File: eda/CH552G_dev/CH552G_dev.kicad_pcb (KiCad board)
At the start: 2 copper layers, 34 x 44 mm, 27 parts, among them IC1 CH552G, J1 USB_B_Micro, J2 Test 1-8, J3 Test 9-16, J4 Battery, SW1 TS2306A, SW11 TS2306A, SW34 TS2306A

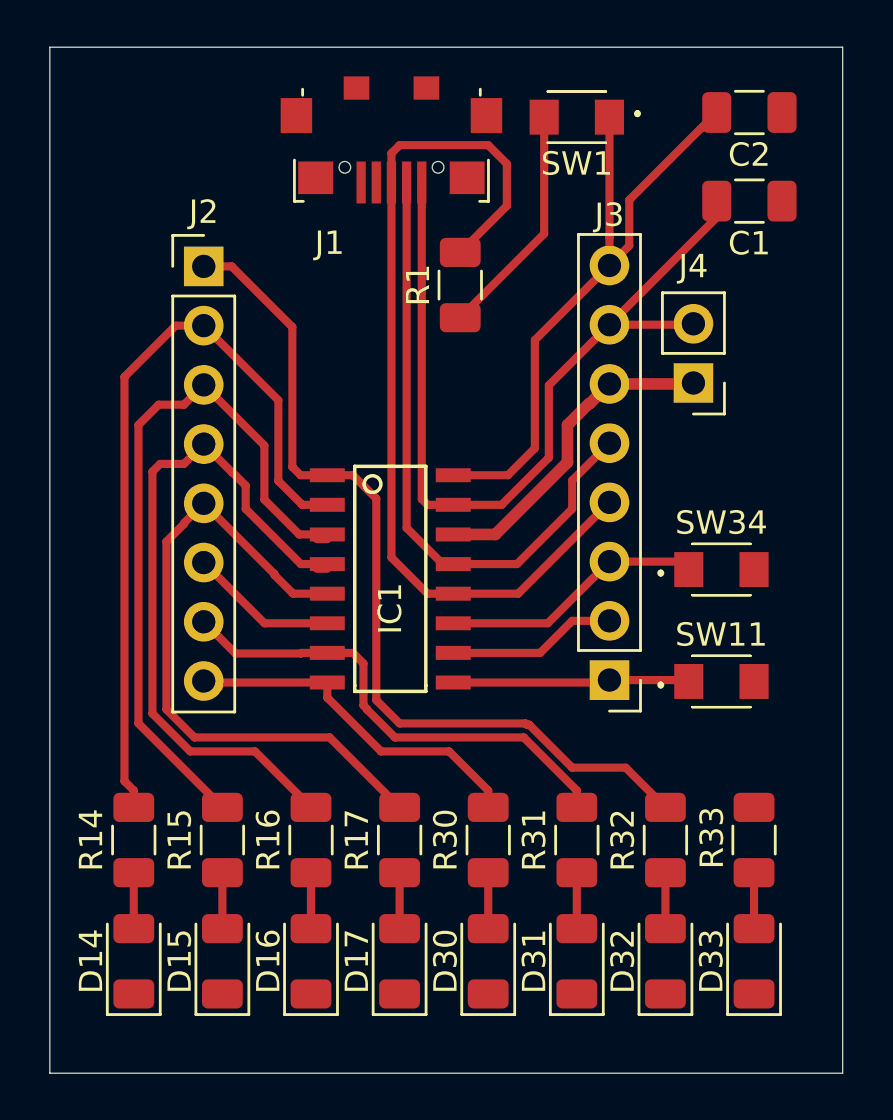
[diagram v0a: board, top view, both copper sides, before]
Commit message: CH552G dev board complete
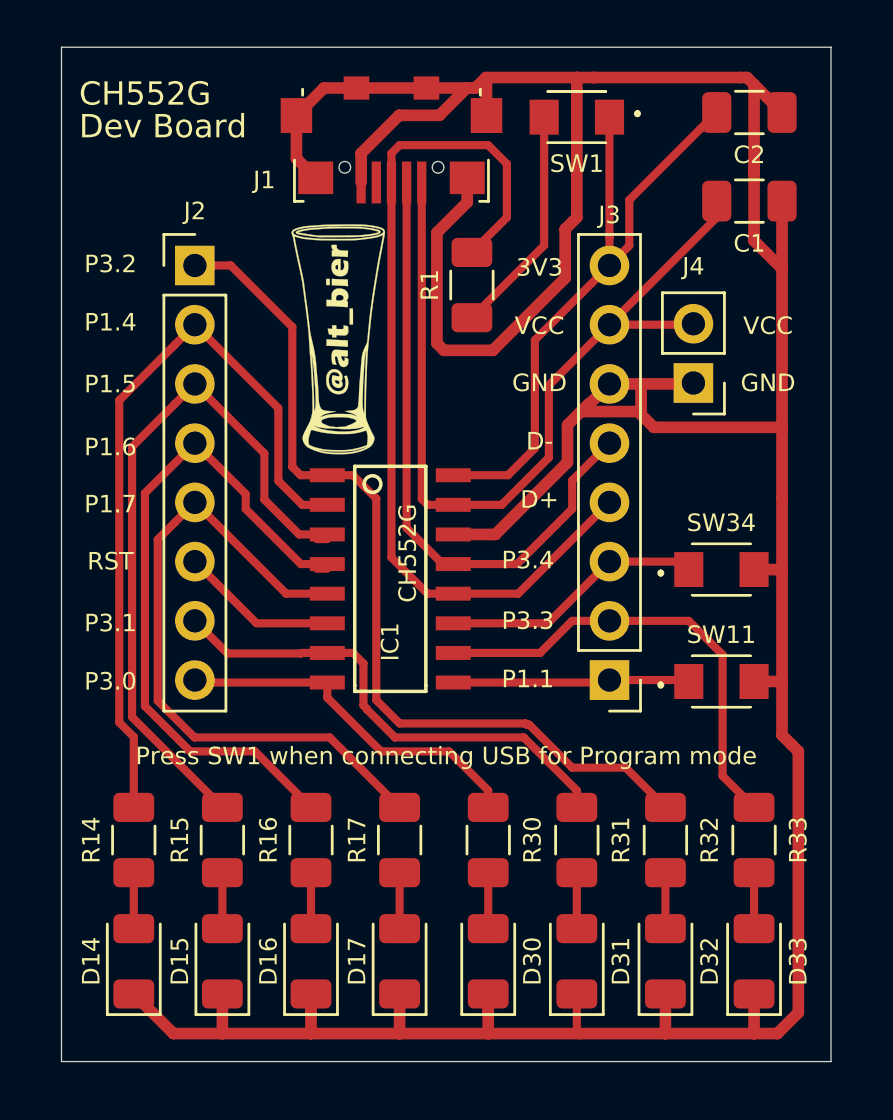
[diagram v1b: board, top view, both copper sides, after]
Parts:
- added G***: LOGO, alt_bier:logo-alt_bier-2300dpi, F.Cu at (106.4, 90.5)
- moved R1 0.50 mm to (112.1, 88.2)
- moved J2 0.38 mm to (100.2, 87.4)
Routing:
- net GND: track 13.9 -> 168.9 mm
- net P3.3: track 7.27 -> 19.8 mm
- net P1.7: track 28.2 -> 28.7 mm
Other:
- board size 34 x 44 mm -> 33 x 43.5 mm
- board text added: "3V3"
- board text added: "CH552G"
- board text added: "D+"
- board text added: "D-"
- board text added: "Dev Board"
- board text added: "GND"
- board text added: "P1.1"
- board text added: "P1.4"
- board text added: "P1.5"
- board text added: "P1.6"
- board text added: "P1.7"
- board text added: "P3.0"
- board text added: "P3.1"
- board text added: "P3.2"
- board text added: "P3.3"
- board text added: "P3.4"
- board text added: "Press SW1 when connecting USB for Program mode"
- board text added: "RST"
- board text added: "VCC"

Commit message: CH552G Dev board update
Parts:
- G***: footprint alt_bier:logo-alt_bier-2300dpi -> alt_bier:logo-alt_bier-2200dpi-4x10mm-front
- moved G*** 0.19 mm to (106.2, 90.5)
